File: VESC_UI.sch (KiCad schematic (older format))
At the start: 60 parts, among them J1 Hall_SS443A, J2 Hall_SS443A, J3 Conn_01x07_Male, J4 Conn_01x09_Female, J5 Conn_01x05_Male, J6 Conn_01x04_Male, J8 Conn_01x02_Male, J9 Conn_01x02_Male, Q1 Q_0010-DVB_Q, Q2 Q_0010-DVB_Q, SW1 SW_Push, SW2 SW_Push, SW3 SW_Push, SW4 SW_Push, SW5 SW_Push, U2 STM32F401CEUx, U3 M95M04-DR, Y1 Crystal_GND24_Small

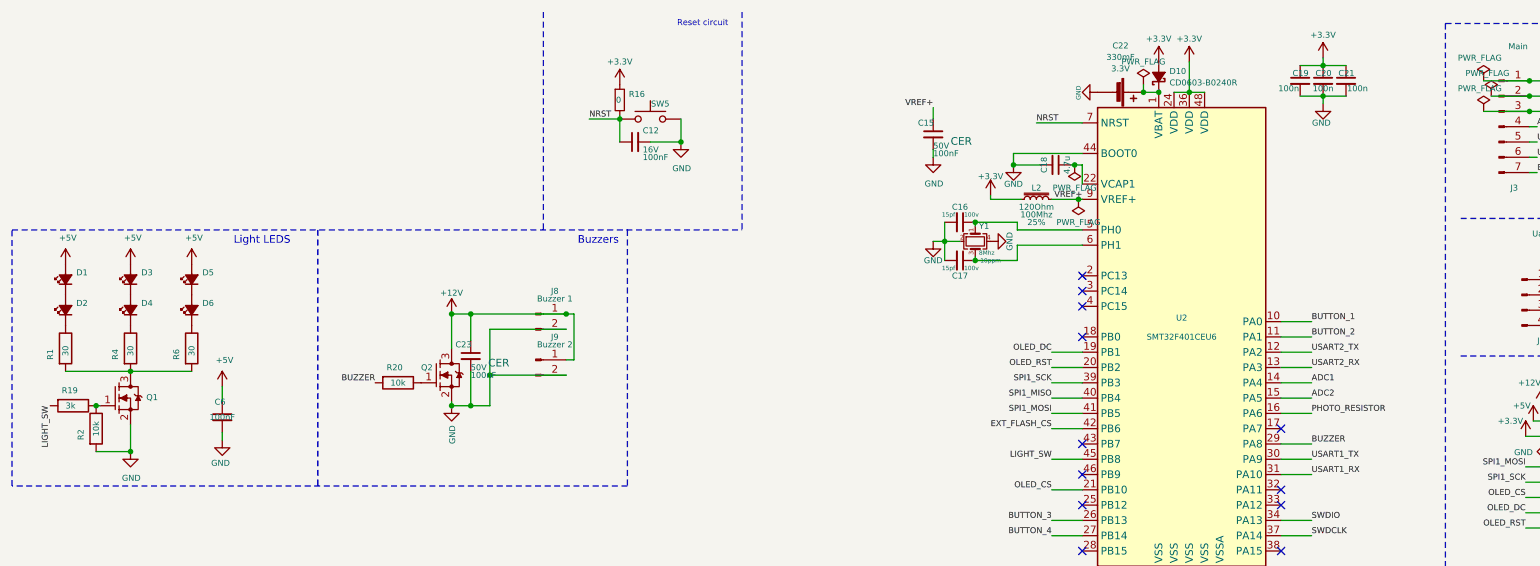
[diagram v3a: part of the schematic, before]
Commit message: fix: add missing rules and components
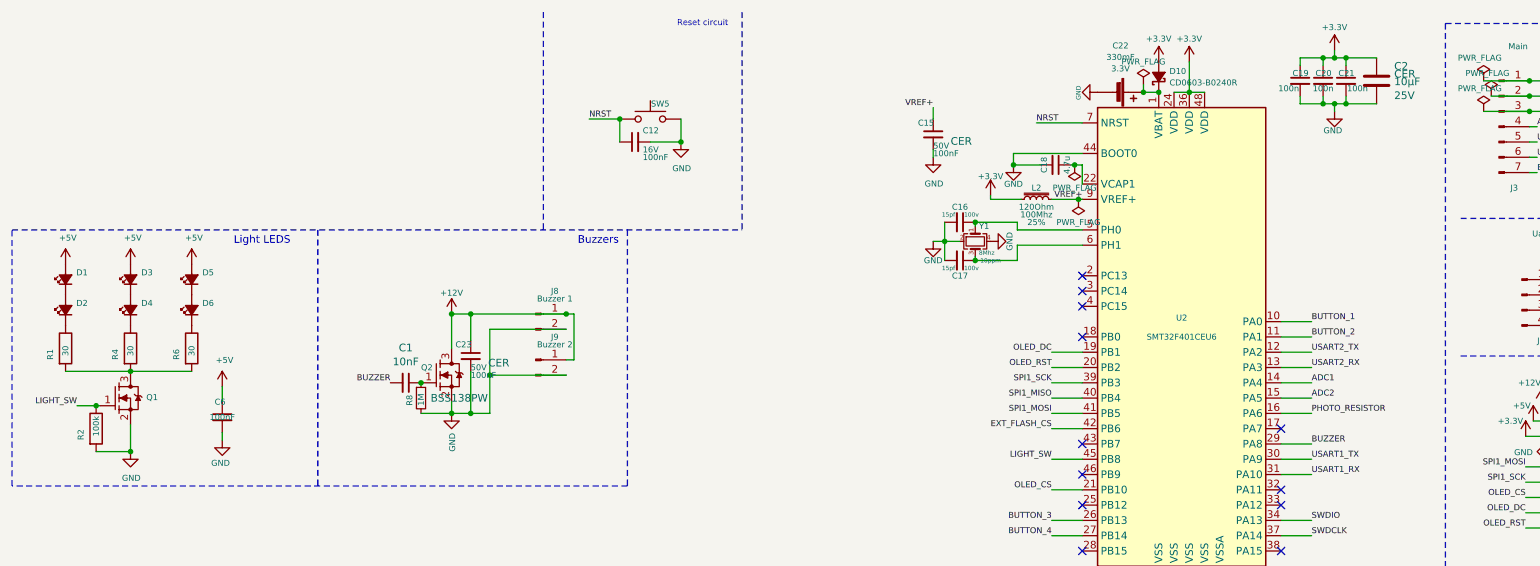
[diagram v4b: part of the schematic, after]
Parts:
- removed R16: R_Small, Resistor_SMD:R_0603_1608Metric_Pad1.05x0.95mm_HandSolder, symbol Device:R_Small
- removed R19, R20: R_0020, Resistor_SMD:R_0603_1608Metric_Pad1.05x0.95mm_HandSolder, symbol Device:R
- added C1: C_Small, Capacitor_SMD:C_0603_1608Metric_Pad1.05x0.95mm_HandSolder, symbol Device:C_Small
- added C2: C_0003-DVB_C, Capacitor_SMD:C_0805_2012Metric_Pad1.15x1.40mm_HandSolder, symbol VESC_UI-rescue:C_0003-DVB_C
- added R8: R_Small, Resistor_SMD:R_0603_1608Metric_Pad1.05x0.95mm_HandSolder, symbol Device:R_Small
- D1, D2, D3, D4, D5, D6: footprint LED_THT:LED_D5.0mm_Clear -> LED_THT:LED_D5.0mm_Horizontal_O1.27mm_Z3.0mm_Clear
- Q2: Field5 50Vds -> 60Vds; Field6 220mA -> 320mA; Field8 (none) -> BSS138PW
- R2: Field4 10k -> 100k
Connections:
- net +3V3: now also C2.1
- net BUZZER: now also C1.2
- net GND: now also C2.2, R8.2
- net LIGHT_SW: now also Q1.1 (G), R2.1
- net at Q2.1 (G): now also C1.1, R8.1
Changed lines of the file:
@@
 F 0 "D1" V 921 2180 39  0000 R CNN
 F 1 "LED_Small_ALT" V 830 2180 39  0001 R CNN
-F 2 "LED_THT:LED_D5.0mm_Clear" V 875 2250 39  0001 C CNN
+F 2 "LED_THT:LED_D5.0mm_Horizontal_O1.27mm_Z3.0mm_Clear" V 875 2250 39  0001 C CNN
 F 3 "~" V 875 2250 39  0001 C CNN
 	1    875  2250
@@
 F 0 "D2" V 921 2380 39  0000 R CNN
 F 1 "LED_Small_ALT" V 830 2380 39  0001 R CNN
-F 2 "LED_THT:LED_D5.0mm_Clear" V 875 2450 39  0001 C CNN
+F 2 "LED_THT:LED_D5.0mm_Horizontal_O1.27mm_Z3.0mm_Clear" V 875 2450 39  0001 C CNN
 F 3 "~" V 875 2450 39  0001 C CNN
 	1    875  2450
@@
 F 0 "D3" V 1346 2180 39  0000 R CNN
 F 1 "LED_Small_ALT" V 1255 2180 39  0001 R CNN
-F 2 "LED_THT:LED_D5.0mm_Clear" V 1300 2250 39  0001 C CNN
+F 2 "LED_THT:LED_D5.0mm_Horizontal_O1.27mm_Z3.0mm_Clear" V 1300 2250 39  0001 C CNN
 F 3 "~" V 1300 2250 39  0001 C CNN
 	1    1300 2250
@@
 F 0 "D4" V 1346 2380 39  0000 R CNN
 F 1 "LED_Small_ALT" V 1255 2380 39  0001 R CNN
-F 2 "LED_THT:LED_D5.0mm_Clear" V 1300 2450 39  0001 C CNN
+F 2 "LED_THT:LED_D5.0mm_Horizontal_O1.27mm_Z3.0mm_Clear" V 1300 2450 39  0001 C CNN
 F 3 "~" V 1300 2450 39  0001 C CNN
 	1    1300 2450
@@
 F 0 "D5" V 1746 2180 39  0000 R CNN
 F 1 "LED_Small_ALT" V 1655 2180 39  0001 R CNN
-F 2 "LED_THT:LED_D5.0mm_Clear" V 1700 2250 39  0001 C CNN
+F 2 "LED_THT:LED_D5.0mm_Horizontal_O1.27mm_Z3.0mm_Clear" V 1700 2250 39  0001 C CNN
 F 3 "~" V 1700 2250 39  0001 C CNN
 	1    1700 2250
@@
 F 0 "D6" V 1746 2380 39  0000 R CNN
 F 1 "LED_Small_ALT" V 1655 2380 39  0001 R CNN
-F 2 "LED_THT:LED_D5.0mm_Clear" V 1700 2450 39  0001 C CNN
+F 2 "LED_THT:LED_D5.0mm_Horizontal_O1.27mm_Z3.0mm_Clear" V 1700 2450 39  0001 C CNN
 F 3 "~" V 1700 2450 39  0001 C CNN
 	1    1700 2450
@@
 F 2 "Resistor_SMD:R_0603_1608Metric_Pad1.05x0.95mm_HandSolder" H 1075 2875 39  0001 C CNN
 F 3 "generic" H 1075 2950 39  0001 C CNN
-F 4 "10k" V 1075 3175 39  0000 L CNN "Field4"
+F 4 "100k" V 1075 3175 39  0000 L CNN "Field4"
 F 5 "1%" V 825 3125 39  0001 L CNN "Field5"
 F 6 "100mW" V 900 3125 39  0001 L CNN "Field6"
@@
 L power:GND #PWR038
 U 1 1 5F86A57C
-P 9100 1100
-F 0 "#PWR038" H 9100 850 39  0001 C CNN
-F 1 "GND" H 9150 975 39  0000 R CNN
-F 2 "" H 9100 1100 39  0001 C CNN
-F 3 "" H 9100 1100 39  0001 C CNN
-	1    9100 1100
-	1    0    0    -1
-$EndComp
-Wire Wire Line
-	9250 1050 9100 1050
-Wire Wire Line
-	8950 1050 9100 1050
-Connection ~ 9100 1050
-Wire Wire Line
-	9100 1100 9100 1050
+P 9175 1150
+F 0 "#PWR038" H 9175 900 39  0001 C CNN
+F 1 "GND" H 9225 1025 39  0000 R CNN
+F 2 "" H 9175 1150 39  0001 C CNN
+F 3 "" H 9175 1150 39  0001 C CNN
+	1    9175 1150
+	1    0    0    -1
+$EndComp
 $Comp
 L power:+3.3V #PWR037
 U 1 1 5F8935F5
-P 9100 800
-F 0 "#PWR037" H 9100 650 39  0001 C CNN
-F 1 "+3.3V" H 9100 950 39  0000 C CNN
-F 2 "" H 9100 800 39  0001 C CNN
-F 3 "" H 9100 800 39  0001 C CNN
-	1    9100 800
-	1    0    0    -1
-$EndComp
-Wire Wire Line
-	8950 850  9100 850
-Wire Wire Line
-	9250 850  9100 850
-Connection ~ 9100 850
-Wire Wire Line
-	9100 800  9100 850
+P 9175 750
+F 0 "#PWR037" H 9175 600 39  0001 C CNN
+F 1 "+3.3V" H 9175 900 39  0000 C CNN
+F 2 "" H 9175 750 39  0001 C CNN
+F 3 "" H 9175 750 39  0001 C CNN
+	1    9175 750
+	1    0    0    -1
+$EndComp
 $Comp
 L Device:C_Small C6
@@
 	7250 1500 7075 1500
 Connection ~ 7075 1500
-$Comp
-L power:+3.3V #PWR024
-U 1 1 5FE23D70
-P 4500 975
-F 0 "#PWR024" H 4500 825 39  0001 C CNN
-F 1 "+3.3V" H 4500 1125 39  0000 C CNN
-F 2 "" H 4500 975 39  0001 C CNN
-F 3 "" H 4500 975 39  0001 C CNN
-	1    4500 975
-	1    0    0    -1
-$EndComp
 Text Label 7225 1225 0    39   ~ 0
 NRST
@@
 Text Label 4300 1200 0    39   ~ 0
 NRST
-$Comp
-L Device:R_Small R16
-U 1 1 5FEB4FA9
-P 4500 1075
-F 0 "R16" H 4559 1113 39  0000 L CNN
-F 1 "R_Small" H 4559 1038 39  0001 L CNN
-F 2 "Resistor_SMD:R_0603_1608Metric_Pad1.05x0.95mm_HandSolder" H 4500 1075 39  0001 C CNN
-F 3 "~" H 4500 1075 39  0001 C CNN
-F 4 "0" H 4475 1075 39  0000 L CNN "Field4"
-	1    4500 1075
-	1    0    0    -1
-$EndComp
-Wire Wire Line
-	4500 1175 4500 1200
 $Comp
 L Switch:SW_Push SW5
@@
 Text Label 7325 2825 2    39   ~ 0
 OLED_RST
-Text Label 775  3075 3    39   ~ 0
+Text Label 950  3075 2    39   ~ 0
 LIGHT_SW
 Text Label 2975 7350 2    39   ~ 0
@@
 F 1 "Q_0010-DVB_Q" H 3300 2635 39  0001 C CNN
 F 2 "Package_TO_SOT_SMD:SOT-23" H 3300 2555 39  0001 C CNN
-F 3 "" H 3300 2485 39  0001 C CNN
+F 3 "https://assets.nexperia.com/documents/data-sheet/BSS138PW.pdf" H 3300 2485 39  0001 C CNN
 F 4 "N-chan" H 3503 2829 39  0001 L CNN "Field1"
 F 5 "MOSFET" H 3300 2045 39  0001 C CNN "Field4"
-F 6 "220mA" H 3300 2195 39  0001 C CNN "Field6"
-F 7 "50Vds" H 3300 2265 39  0001 C CNN "Field5"
+F 6 "320mA" H 3300 2195 39  0001 C CNN "Field6"
+F 7 "60Vds" H 3300 2265 39  0001 C CNN "Field5"
+F 8 "BSS138PW" H 3450 2725 50  0000 C CNN "Field8"
 	1    3300 2875
 	1    0    0    -1
@@
 L power:GND #PWR053
 U 1 1 5FAA3E1F
-P 3400 3075
-F 0 "#PWR053" H 3400 2825 39  0001 C CNN
-F 1 "GND" V 3405 2947 39  0000 R CNN
-F 2 "" H 3400 3075 39  0001 C CNN
-F 3 "" H 3400 3075 39  0001 C CNN
-	1    3400 3075
-	1    0    0    -1
-$EndComp
-$Comp
-L Device:R R19
-U 1 1 5FAA4707
-P 925 3075
-F 0 "R19" V 825 3000 39  0000 L CNN
-F 1 "R_0020" H 925 2875 39  0001 C CNN
-F 2 "Resistor_SMD:R_0603_1608Metric_Pad1.05x0.95mm_HandSolder" H 925 2725 39  0001 C CNN
-F 3 "generic" H 925 2800 39  0001 C CNN
-F 4 "3k" V 925 3025 39  0000 L CNN "Field4"
-F 5 "1%" V 675 2975 39  0001 L CNN "Field5"
-F 6 "100mW" V 750 2975 39  0001 L CNN "Field6"
-	1    925  3075
-	0    1    1    0
-$EndComp
-Connection ~ 1075 3075
-$Comp
-L Device:R R20
-U 1 1 5FAA5C52
-P 3050 2925
-F 0 "R20" V 2950 2850 39  0000 L CNN
-F 1 "R_0020" H 3050 2725 39  0001 C CNN
-F 2 "Resistor_SMD:R_0603_1608Metric_Pad1.05x0.95mm_HandSolder" H 3050 2575 39  0001 C CNN
-F 3 "generic" H 3050 2650 39  0001 C CNN
-F 4 "10k" V 3050 2875 39  0000 L CNN "Field4"
-F 5 "1%" V 2800 2825 39  0001 L CNN "Field5"
-F 6 "100mW" V 2875 2825 39  0001 L CNN "Field6"
-	1    3050 2925
-	0    1    1    0
+P 3400 3125
+F 0 "#PWR053" H 3400 2875 39  0001 C CNN
+F 1 "GND" V 3405 2997 39  0000 R CNN
+F 2 "" H 3400 3125 39  0001 C CNN
+F 3 "" H 3400 3125 39  0001 C CNN
+	1    3400 3125
+	1    0    0    -1
 $EndComp
 Text Label 9025 3325 0    39   ~ 0
 BUZZER
-Text Label 2900 2925 2    39   ~ 0
+Text Label 3000 2925 2    39   ~ 0
 BUZZER
 Wire Wire Line
 	4150 2875 3650 2875
-Wire Wire Line
-	3400 3075 3400 3050
-Wire Wire Line
-	3650 3075 3525 3075
-Wire Wire Line
-	3650 2875 3650 3075
-Connection ~ 3400 3075
 Wire Wire Line
 	3650 2875 3650 2575
@@
 	3525 2475 3400 2475
 Wire Wire Line
-	3525 2850 3525 3075
-Connection ~ 3525 3075
-Wire Wire Line
-	3525 3075 3400 3075
-Wire Wire Line
 	10450 1250 10500 1250
 Wire Wire Line
@@
 Wire Wire Line
 	10425 3475 10600 3475
+Wire Wire Line
+	1075 3075 950  3075
+Connection ~ 1075 3075
+$Comp
+L VESC_UI-rescue:C_0003-DVB_C C2
+U 1 1 5FD74130
+P 9450 950
+F 0 "C2" H 9565 1046 50  0000 L CNN
+F 1 "C_0003-DVB_C" H 9450 650 50  0001 C CNN
+F 2 "Capacitor_SMD:C_0805_2012Metric_Pad1.15x1.40mm_HandSolder" H 9450 500 50  0001 C CNN
+F 3 "" H 9450 575 50  0001 C CNN
+F 4 "CER" H 9565 995 0   0000 L CNN "Field4"
+F 5 "10µF" H 9565 945 50  0000 L CNN "Field5"
+F 6 "25V" H 9565 854 50  0000 L CNN "Field6"
+F 7 "X5R" H 9550 800 60  0001 L CNN "Field7"
+F 8 "10%" H 9550 725 60  0001 L CNN "Field8"
+	1    9450 950
+	1    0    0    -1
+$EndComp
+Wire Wire Line
+	9450 800  9250 800
+Wire Wire Line
+	8950 800  8950 850
+Wire Wire Line
+	9100 850  9100 800
+Connection ~ 9100 800
+Wire Wire Line
+	9100 800  8950 800
+Wire Wire Line
+	9250 850  9250 800
+Connection ~ 9250 800
+Wire Wire Line
+	9250 800  9175 800
+Wire Wire Line
+	9450 1100 9250 1100
+Wire Wire Line
+	8950 1100 8950 1050
+Wire Wire Line
+	9100 1050 9100 1100
+Connection ~ 9100 1100
+Wire Wire Line
+	9100 1100 8950 1100
+Wire Wire Line
+	9250 1050 9250 1100
+Connection ~ 9250 1100
+Wire Wire Line
+	9250 1100 9175 1100
+Wire Wire Line
+	9175 1150 9175 1100
+Connection ~ 9175 1100
+Wire Wire Line
+	9175 1100 9100 1100
+Wire Wire Line
+	9175 750  9175 800
+Connection ~ 9175 800
+Wire Wire Line
+	9175 800  9100 800
+$Comp
+L Device:C_Small C1
+U 1 1 5FDC019E
+P 3100 2925
+F 0 "C1" V 2871 2925 50  0000 C CNN
+F 1 "C_Small" V 2962 2925 50  0001 C CNN
+F 2 "Capacitor_SMD:C_0603_1608Metric_Pad1.05x0.95mm_HandSolder" H 3100 2925 50  0001 C CNN
+F 3 "~" H 3100 2925 50  0001 C CNN
+F 4 "10nF" V 2962 2925 50  0000 C CNN "Field4"
+	1    3100 2925
+	0    1    1    0
+$EndComp
+Connection ~ 3200 2925
+Wire Wire Line
+	3200 3125 3400 3125
+Wire Wire Line
+	3400 3050 3400 3125
+Connection ~ 3400 3125
+Wire Wire Line
+	3525 3125 3400 3125
+Wire Wire Line
+	3525 2850 3525 3125
+Wire Wire Line
+	3650 3125 3525 3125
+Wire Wire Line
+	3650 2875 3650 3125
+Connection ~ 3525 3125
+$Comp
+L Device:R_Small R8
+U 1 1 5FDC1B3C
+P 3200 3025
+F 0 "R8" V 3125 2975 39  0000 L CNN
+F 1 "R_Small" H 3259 2980 39  0001 L CNN
+F 2 "Resistor_SMD:R_0603_1608Metric_Pad1.05x0.95mm_HandSolder" H 3200 3025 39  0001 C CNN
+F 3 "~" H 3200 3025 39  0001 C CNN
+F 4 "1M" V 3200 2975 39  0000 L CNN "Field4"
+F 5 "1%" H 3200 3025 39  0001 C CNN "Field5"
+	1    3200 3025
+	1    0    0    -1
+$EndComp
 $EndSCHEMATC

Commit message: fix: change screen connector footprint and adjust its mechanical position
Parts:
- J4: footprint Connector_PinHeader_1.27mm:PinHeader_1x09_P1.27mm_Vertical -> Connector_PinHeader_2.00mm:PinHeader_1x09_P2.00mm_Vertical
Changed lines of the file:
@@
 F 0 "J4" H 10828 3501 50  0000 L CNN
 F 1 "Conn_01x09_Female" H 10828 3410 50  0000 L CNN
-F 2 "Connector_PinHeader_1.27mm:PinHeader_1x09_P1.27mm_Vertical" H 10800 3475 50  0001 C CNN
+F 2 "Connector_PinHeader_2.00mm:PinHeader_1x09_P2.00mm_Vertical" H 10800 3475 50  0001 C CNN
 F 3 "~" H 10800 3475 50  0001 C CNN
 	1    10800 3475
